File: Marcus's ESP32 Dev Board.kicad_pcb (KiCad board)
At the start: 6 copper layers, 26.8 x 22.4 mm, 71 parts, among them J1 SM02B-SRSS-TB(LF)(SN), J2 USB_B_Micro, J4 Conn_01x16, U1 ESP32-S3-WROOM-1, U11 BMP390, U13 TPS63020DSJR, U4 MMC5983MA, U5 AP2112K-3.3, U6 DRV2605LDGS, U7 DRV2605LDGS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

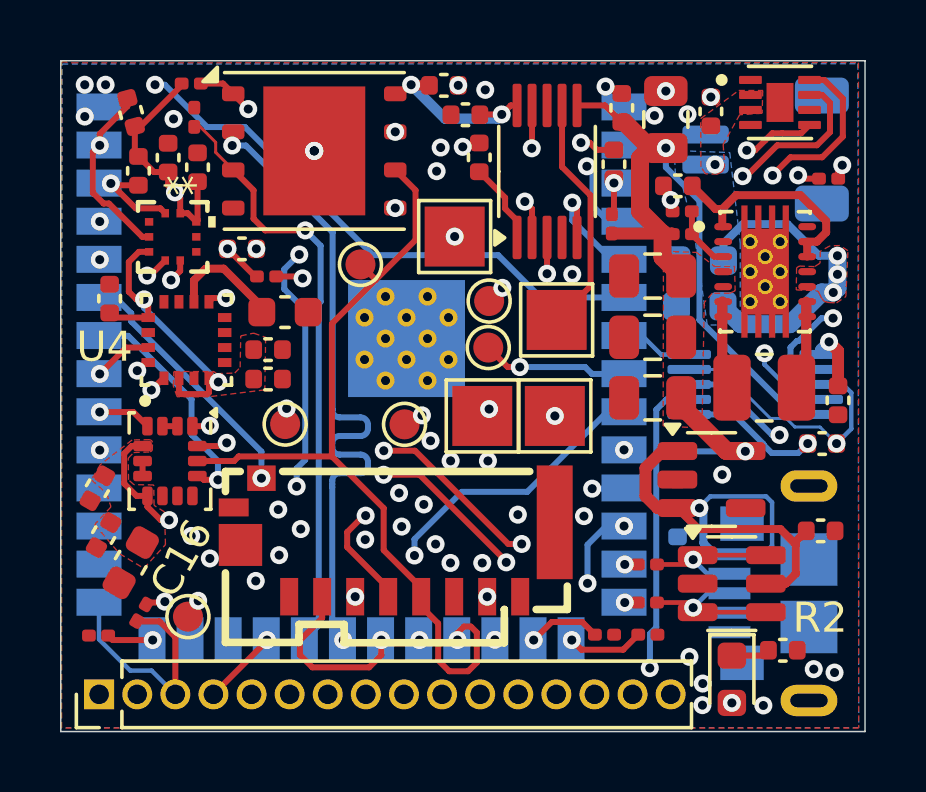
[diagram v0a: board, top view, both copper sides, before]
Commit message: feat(pcb) length match battery sensor i2c
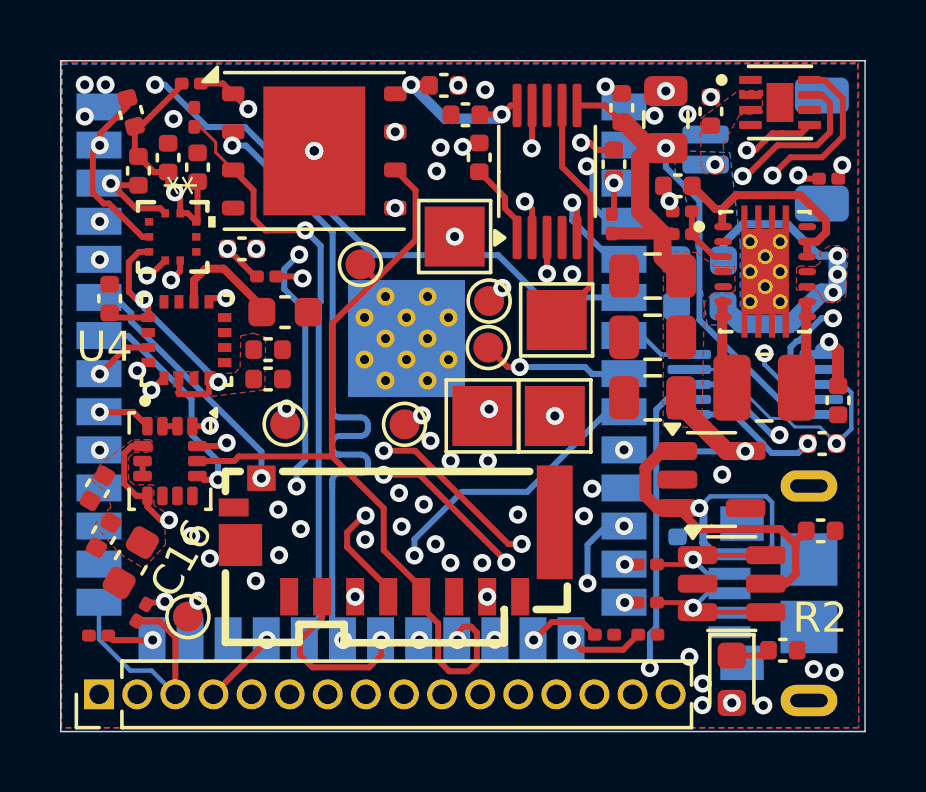
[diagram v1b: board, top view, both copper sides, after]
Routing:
- net /I2C1 SDA: track 89.5 -> 92.4 mm

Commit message: feat(pcb) add pullups to I2C0, move battery sensor to I2C0
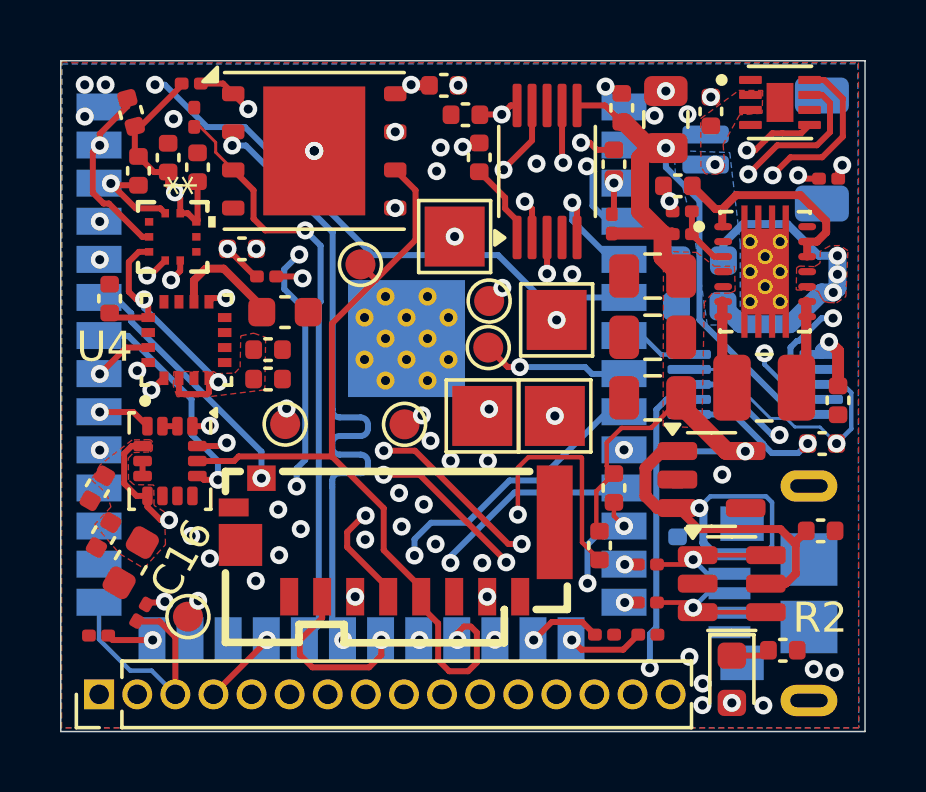
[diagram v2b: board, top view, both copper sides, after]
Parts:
- added R11: 2k7R, Capacitor_SMD:C_0402_1005Metric, F.Cu at (92.8, 78.3)
- added R13: 2k7R, Capacitor_SMD:C_0402_1005Metric, F.Cu at (92.4, 80.2)
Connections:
- U8 pad 7: /I2C1 SCL -> /I2C0 SCL
- U8 pad 8: /I2C1 SDA -> /I2C0 SDA
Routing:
- net /I2C1 SDA: track 92.4 -> 53.0 mm, vias 6 -> 5
- net /I2C1 SCL: track 79.0 -> 46.4 mm, vias 6 -> 4
- net /I2C0 SCL: track 25.0 -> 47.2 mm, vias 3 -> 4
- net /I2C0 SDA: track 32.7 -> 48.4 mm, vias 3 -> 4
- net /HAPTIC2+: track 8.01 -> 12.0 mm, vias 0 -> 2
- net +3.3V: track 96.3 -> 99.2 mm
- net /GPIO18: track 12.3 -> 12.0 mm, vias 2 -> 1

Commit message: feat(pcb) cleanup and improve reliability
add pullups to SPI CS lines, rearrange board slightly, add V1.0 silkscreen, increase size of VBUS input cap
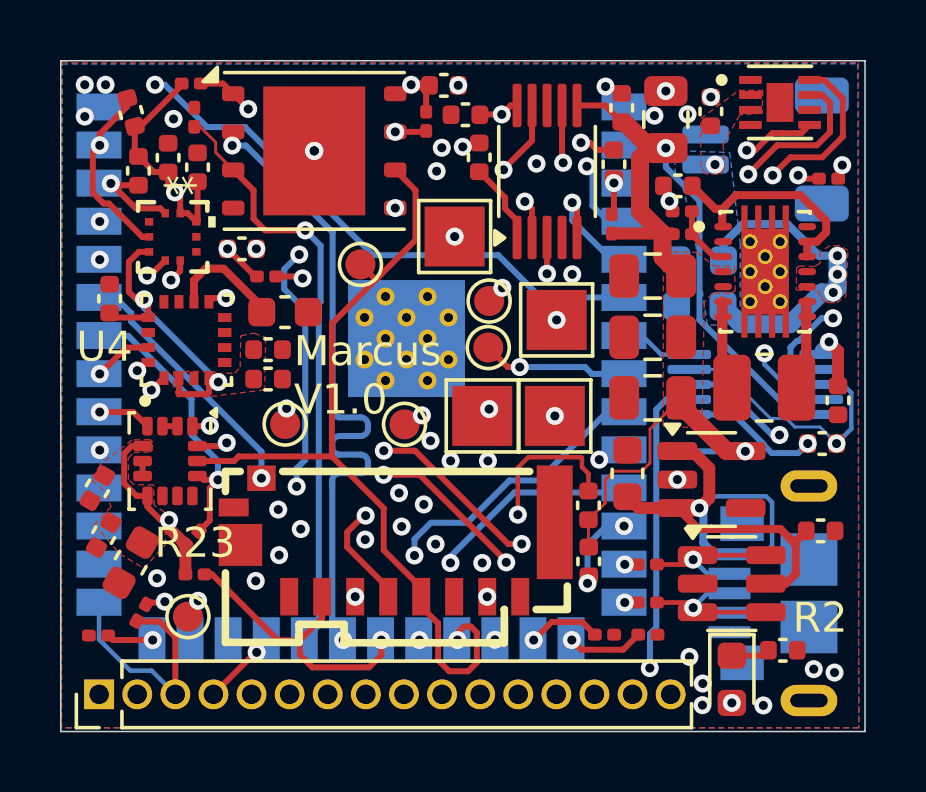
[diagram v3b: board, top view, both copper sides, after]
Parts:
- removed C11: 1uF, Capacitor_SMD:C_0402_1005Metric
- added C41: 10uF, Capacitor_SMD:C_0603_1608Metric, F.Cu at (93.3, 77.8)
- added R21: 10kR, Resistor_SMD:R_0201_0603Metric, F.Cu at (86.6, 66.1)
- added R22: 10kR, Resistor_SMD:R_0201_0603Metric, F.Cu at (78.8, 80.0)
- added R23: 10kR, Resistor_SMD:R_0201_0603Metric, F.Cu at (78.9, 81.2)
- moved R11 2.59 mm to (92.0, 80.8)
- moved R13 1.39 mm to (92.0, 78.9), turned to -90 degrees
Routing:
- net /SPI2 CS2: track 5.81 -> 9.89 mm
- net +3.3V: track 99.2 -> 102.5 mm
- net /I2C0 SCL: track 47.2 -> 44.8 mm
- net /SPI2 CS0: track 7.73 -> 9.70 mm
- net VBUS: track 20.7 -> 21.9 mm
- net /FLASH HOLD: track 14.5 -> 15.6 mm
- net /I2C0 SDA: track 48.4 -> 47.7 mm
- net /GPIO17: track 13.7 -> 13.1 mm
- net GND: vias 39 -> 38
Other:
- board text added: "Marcus V1.0"
